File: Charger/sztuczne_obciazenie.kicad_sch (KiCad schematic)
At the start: 25 parts, among them Q13 BC846BW, Q14 Q_NPN_BCE, Q15 Q_NPN_BCE, Q16 Q_NPN_BCE, U10 MCP6001-OT, U11 MCP6001-OT, U7 MCP6001-OT, U8 MCP6001-OT, U9 MCP6001-OT

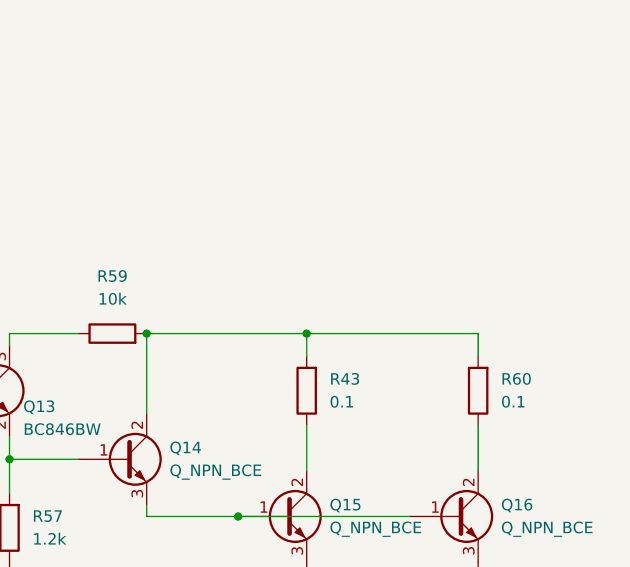
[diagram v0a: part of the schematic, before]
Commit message: Update sztuczne_obciazenie.kicad_sch
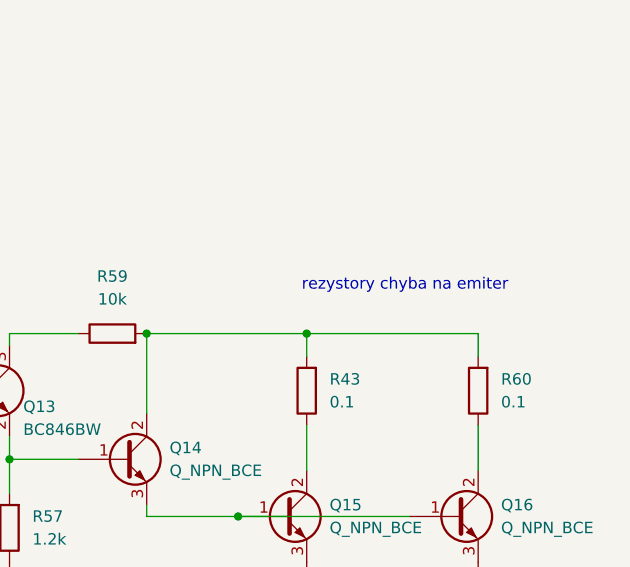
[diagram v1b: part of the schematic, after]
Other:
- note added: "rezystory chyba na emiter"
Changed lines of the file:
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@@
+		)
+	)
+	(text "rezystory chyba na emiter\n"
+		(exclude_from_sim no)
+		(at 230.632 77.216 0)
+		(effects
+			(font
+				(size 1.27 1.27)
+			)
 		)
 	)

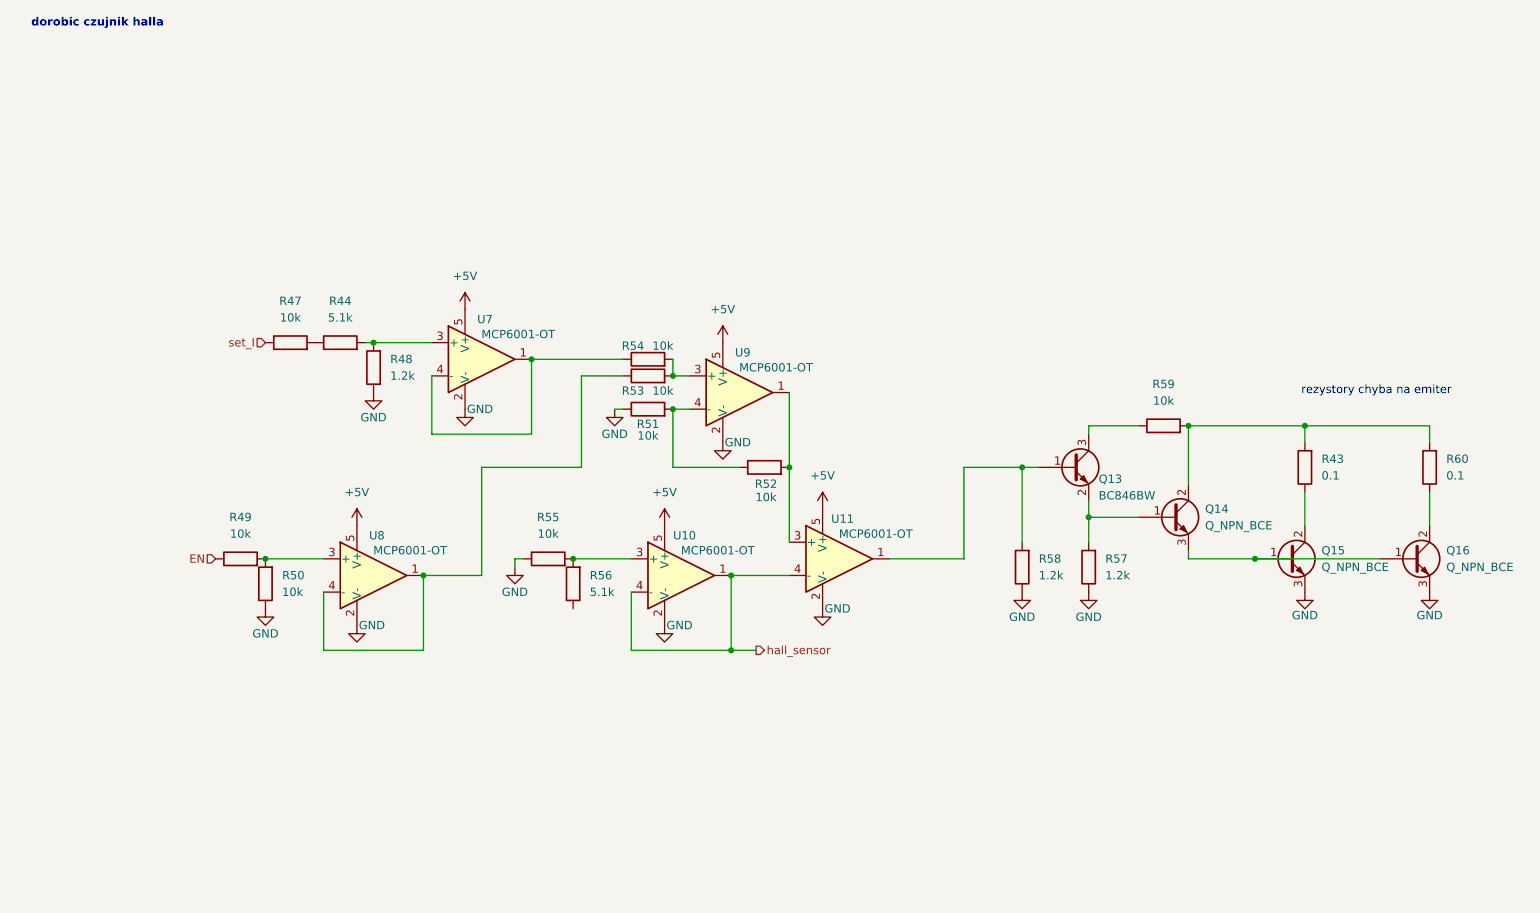
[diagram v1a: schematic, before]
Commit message: powiar rw + zlacze baterii
koniecznie sprawdzić masy i flagi
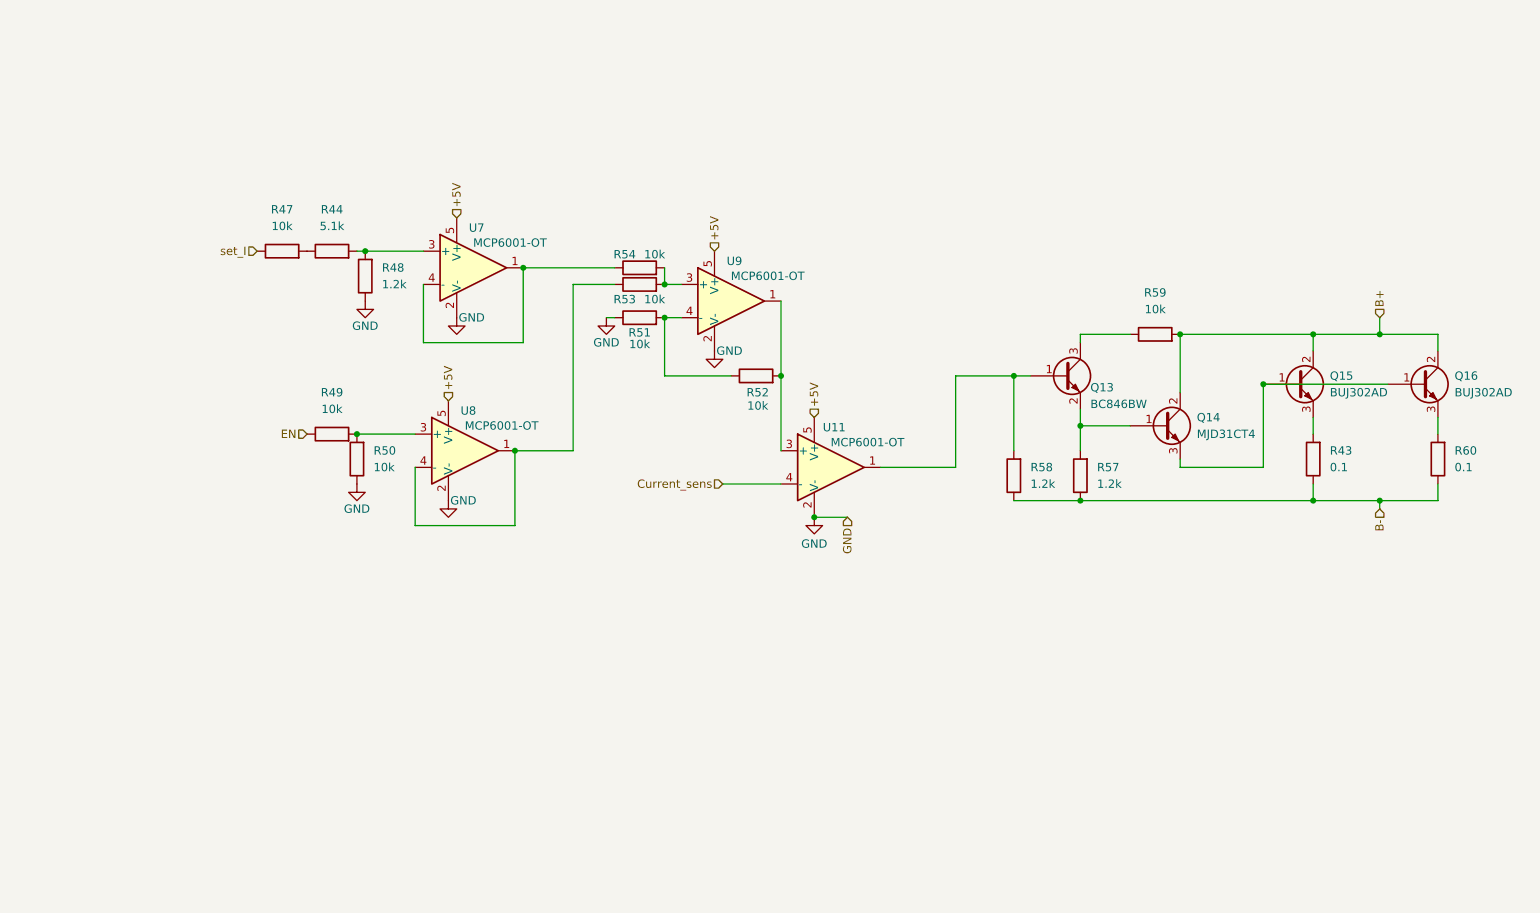
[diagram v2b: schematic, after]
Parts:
- removed R55: 10k, symbol Device:R
- removed R56: 5.1k, symbol Device:R
- removed U10: MCP6001-OT, Package_TO_SOT_SMD:SOT-23-5, symbol Amplifier_Operational:MCP6001-OT
- Q14: value Q_NPN_BCE -> MJD31CT4
- Q15, Q16: value Q_NPN_BCE -> BUJ302AD
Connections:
- net GND: no longer Q15.3 (E), Q16.3 (E), R57.1, R58.1
- net B+: now reaches Q14.2 (C), R59.2
- net B+: now also Q15.2 (C), Q16.2 (C); no longer R43.2, R60.2
- net B-: now reaches R60.1
- net B-: now also R43.1, R57.1, R58.1; no longer Q16.2 (C)
- net hall_sensor renamed Current_sens
- new net: Q15.3 (E), R43.2
- new net: Q16.3 (E), R60.2
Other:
- note removed: "dorobic czujnik halla"
- note removed: "rezystory chyba na emiter"
- moved on the sheet: Q13, Q14, Q15, Q16, R44, R47, R48, R49, R50, R51, R52, R53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

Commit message: update
zakonczony schemat balansera, sztucznego obciazenia i pomiaru pradu. Przypisane wszystkie footprinty
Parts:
- added C12, C13, C14, C15: 100n, Capacitor_SMD:C_0805_2012Metric_Pad1.18x1.45mm_HandSolder, symbol Device:C
- Q14, Q15, Q16: footprint (none) -> Package_TO_SOT_SMD:TO-252-2
- R43, R60: footprint (none) -> Resistor_SMD:R_1206_3216Metric_Pad1.30x1.75mm_HandSolder
- R44, R47, R48, R49, R50, R51, R52, R53, R54, R57, R58, R59: footprint (none) -> Resistor_SMD:R_0805_2012Metric_Pad1.20x1.40mm_HandSolder
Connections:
- net B- is gone; now on net GND: R43.1, R57.1, R58.1, R60.1
- net +5V: now also C12.1, C13.1, C14.1, C15.1
- net GND: now also C12.2, C13.2, C14.2, C15.2
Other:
- moved on the sheet: Q13, Q14, Q15, Q16, R43, R44, R47, R48, R49, R50, R51, R52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
